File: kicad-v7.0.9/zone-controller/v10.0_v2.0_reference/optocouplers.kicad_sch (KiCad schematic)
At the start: 108 parts, among them U1 TLP2345, U10 TLP2345, U11 TLP2345, U12 TLP2345, U13 TLP2345, U14 TLP2345, U2 TLP2345, U5 TLP2345, U6 TLP2345, U7 TLP2345, U8 TLP2345, U9 TLP2345

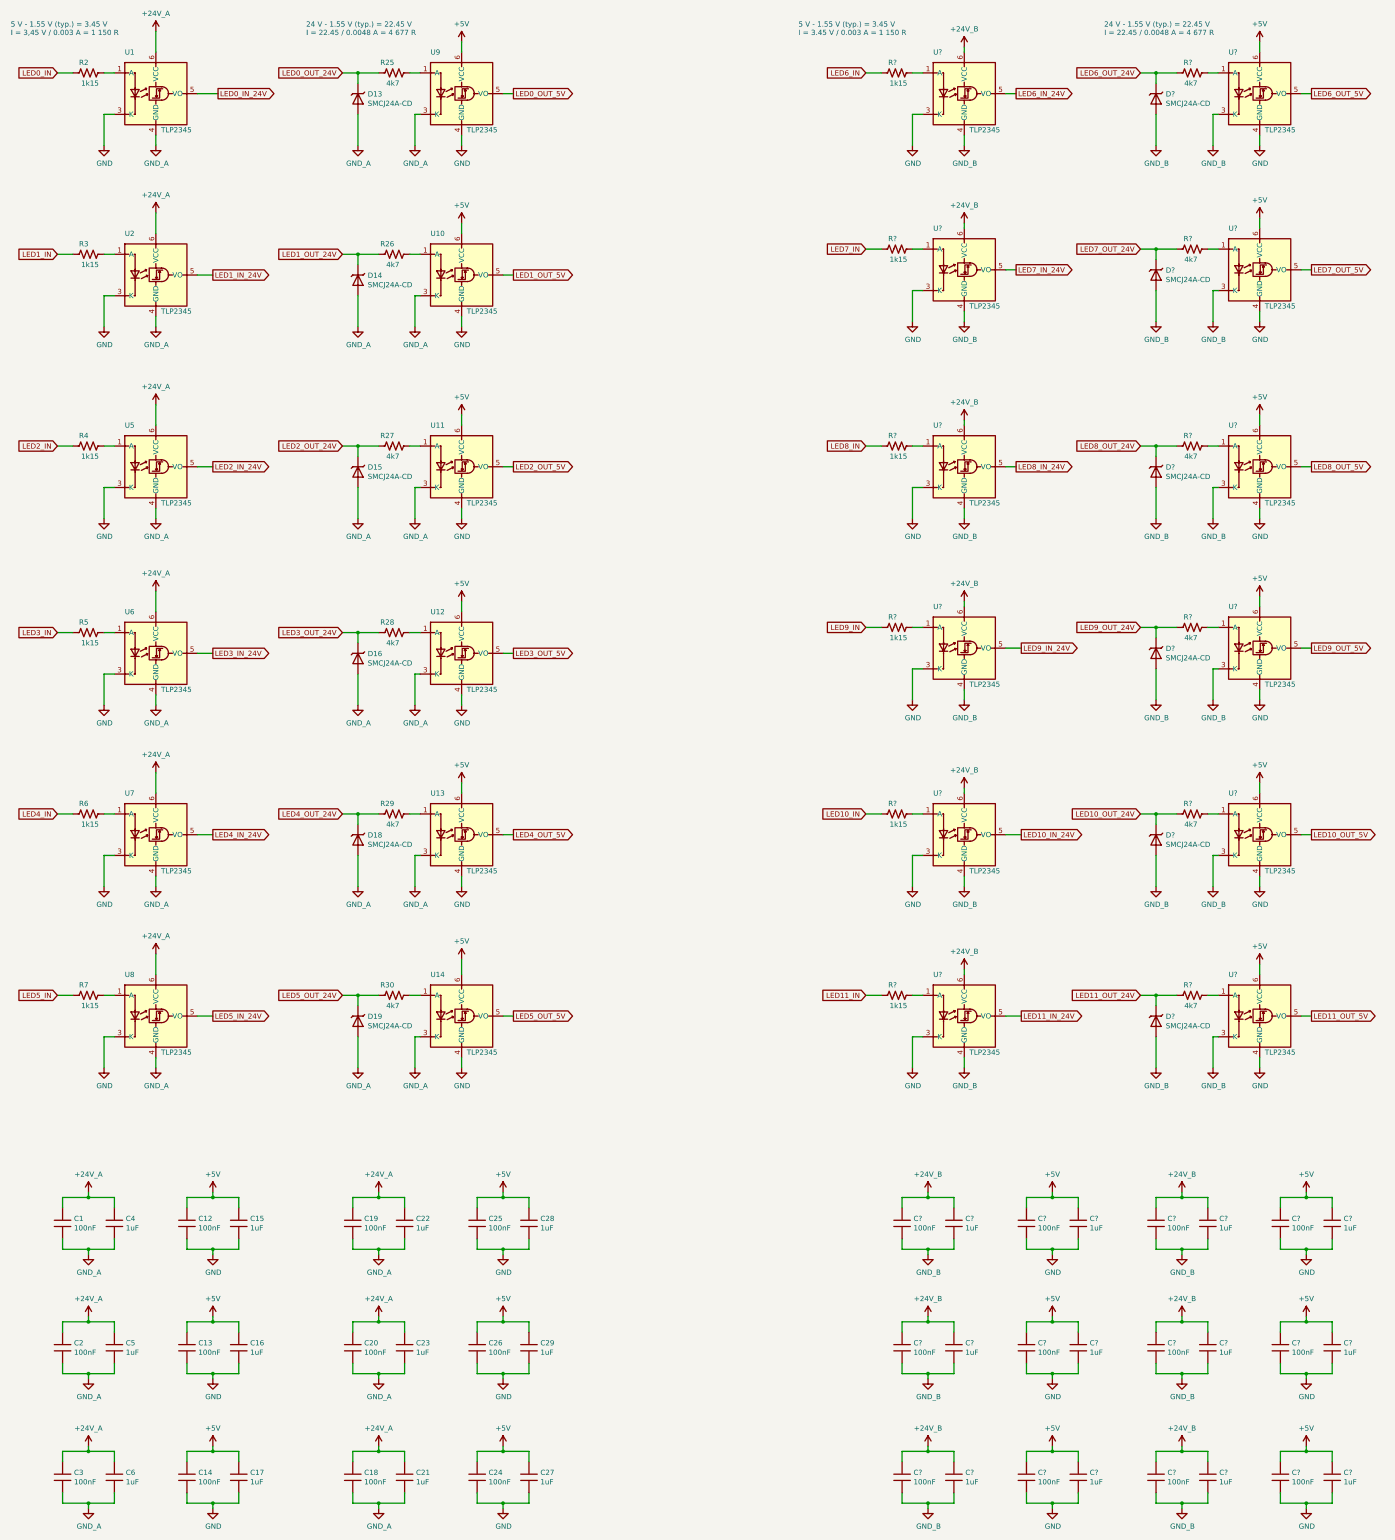
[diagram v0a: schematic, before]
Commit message: Zone controller. Change library. Small changes in schematic a PCB.
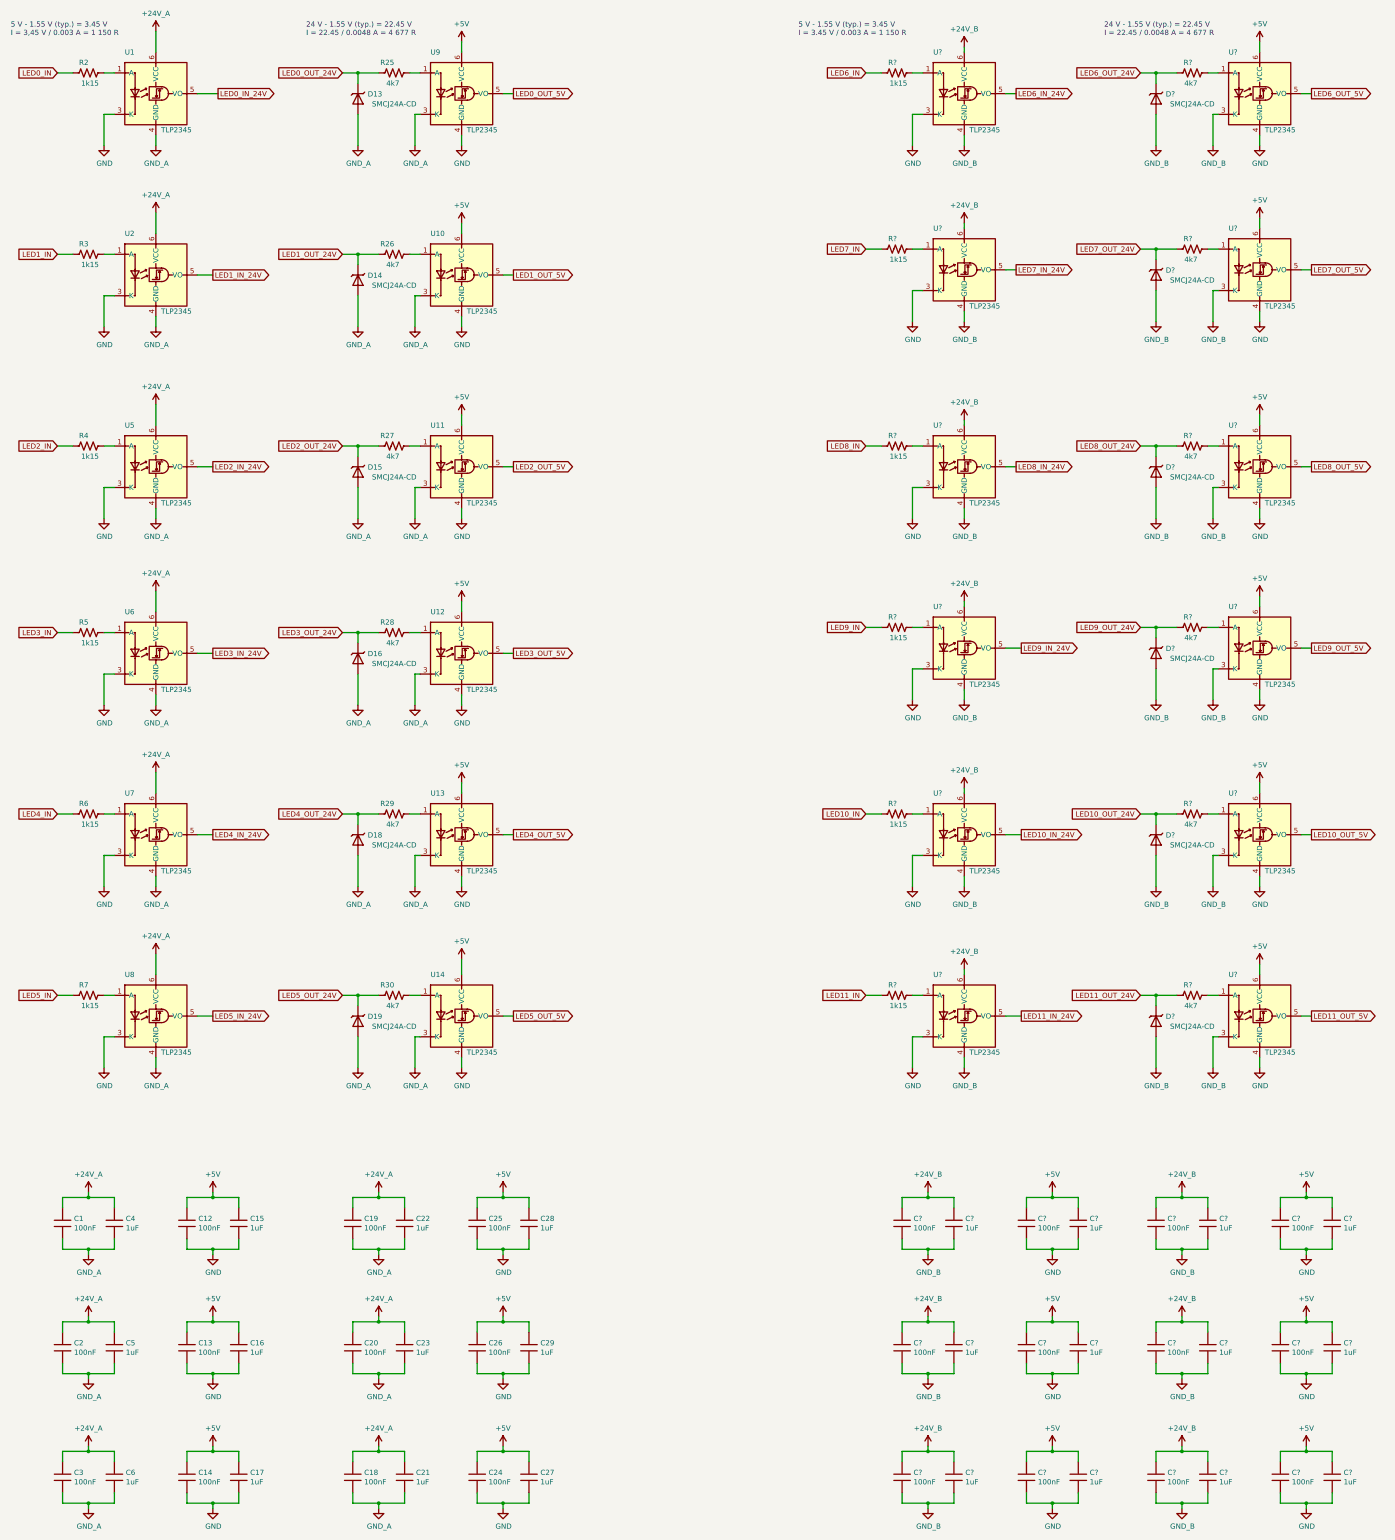
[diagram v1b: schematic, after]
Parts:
- C1, C12, C13, C14, C15, C16, C17, C18, C19, C2, C20, C21, C22, C23, C24, C25, C26, C27, C28, C29, C3, C4, C5, C6, C? (x24): symbol passive_component_rl:capacitor -> capacitor_smd_rl:c_1206
- D13, D14, D15, D16, D18, D19, D? (x6): symbol diode_rl:undir_transil -> transil_diode_smd_rl:SMCJ24A-CD
- R2, R25, R26, R27, R28, R29, R3, R30, R4, R5, R6, R7, R? (x12): symbol passive_component_rl:resistor_us -> resistor_smd_rl:r_1206_us
- U1, U10, U11, U12, U13, U14, U2, U5, U6, U7, U8, U9, U? (x12): symbol optocoupler_rl:TLP2345 -> optocoupler_smd_rl:TLP2345
